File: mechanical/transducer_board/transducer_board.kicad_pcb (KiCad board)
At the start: 2 copper layers, 66.6 x 66.6 mm, 65 parts, among them J1 Conn_02x17_Odd_Even, J2 Conn_01x01, J3 Conn_01x01, J4 Conn_01x01, U1 XL62783, U2 XL62083, U3 XL62783, U4 XL62083

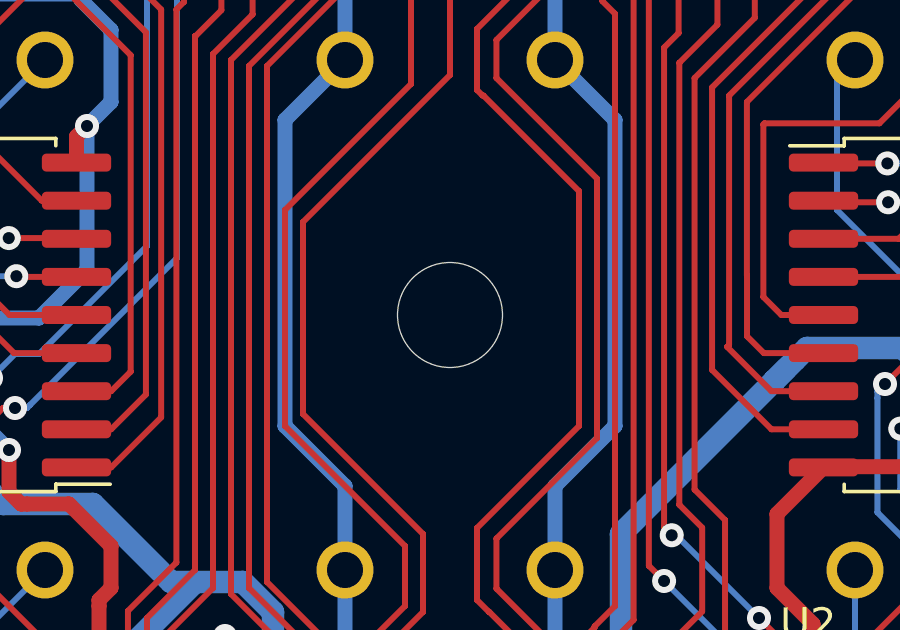
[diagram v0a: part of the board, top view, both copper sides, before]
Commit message: Tightened transducer board mounting hole size
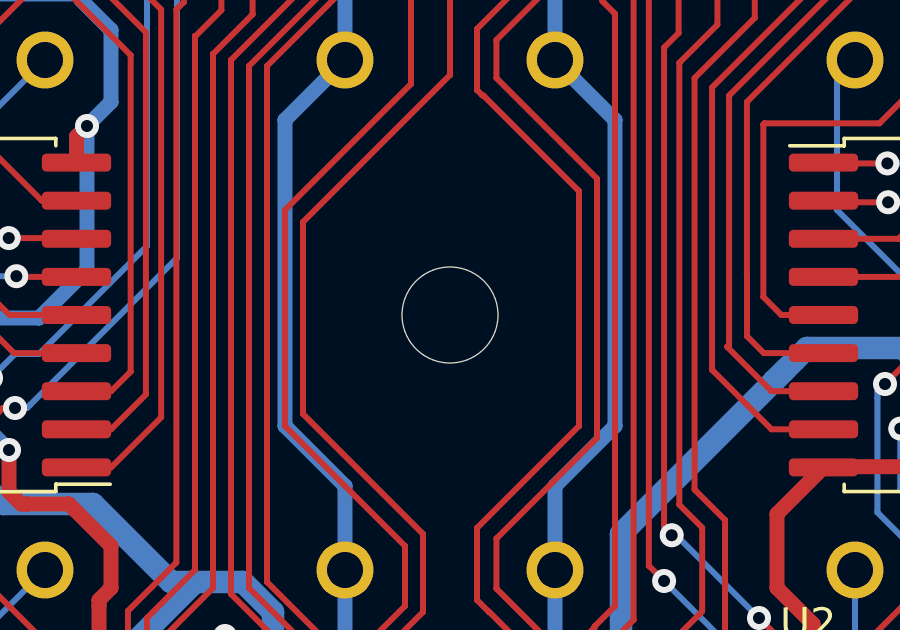
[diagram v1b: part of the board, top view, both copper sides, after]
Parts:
- REF**: value MountingHole_3.5mm -> MountingHole_3.2mm_M3; footprint MountingHole:MountingHole_3.5mm -> MountingHole:MountingHole_3.2mm_M3

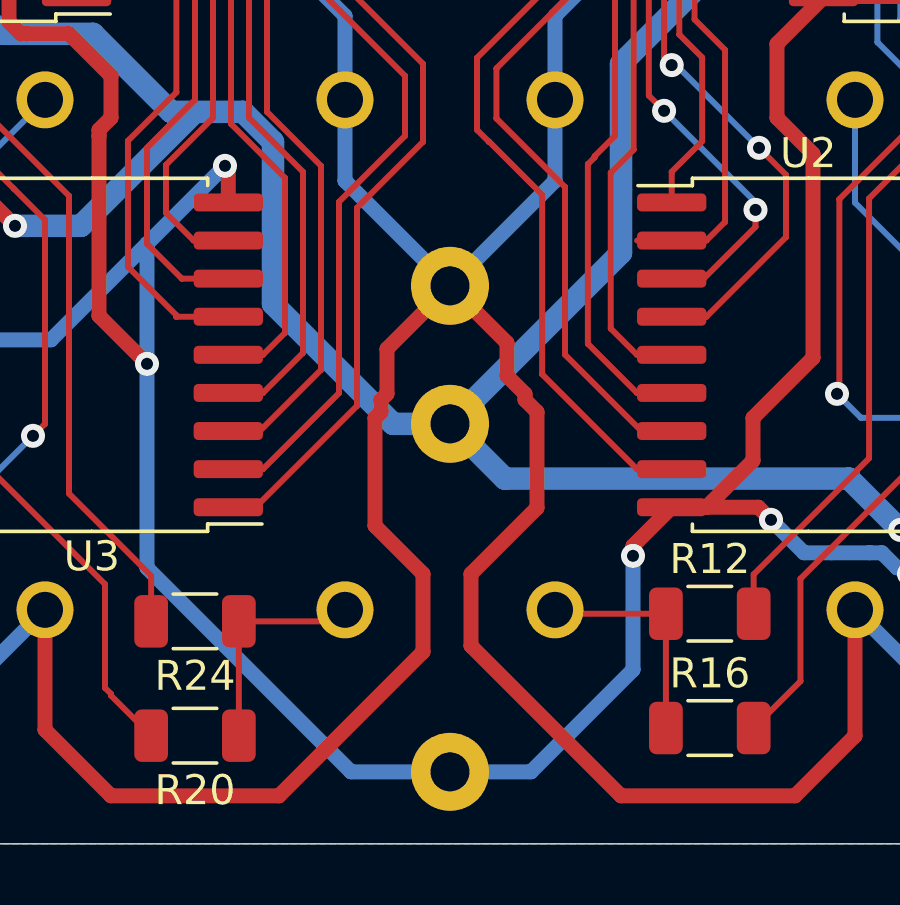
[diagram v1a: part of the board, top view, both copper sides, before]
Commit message: Clearly mark which power wire goes where
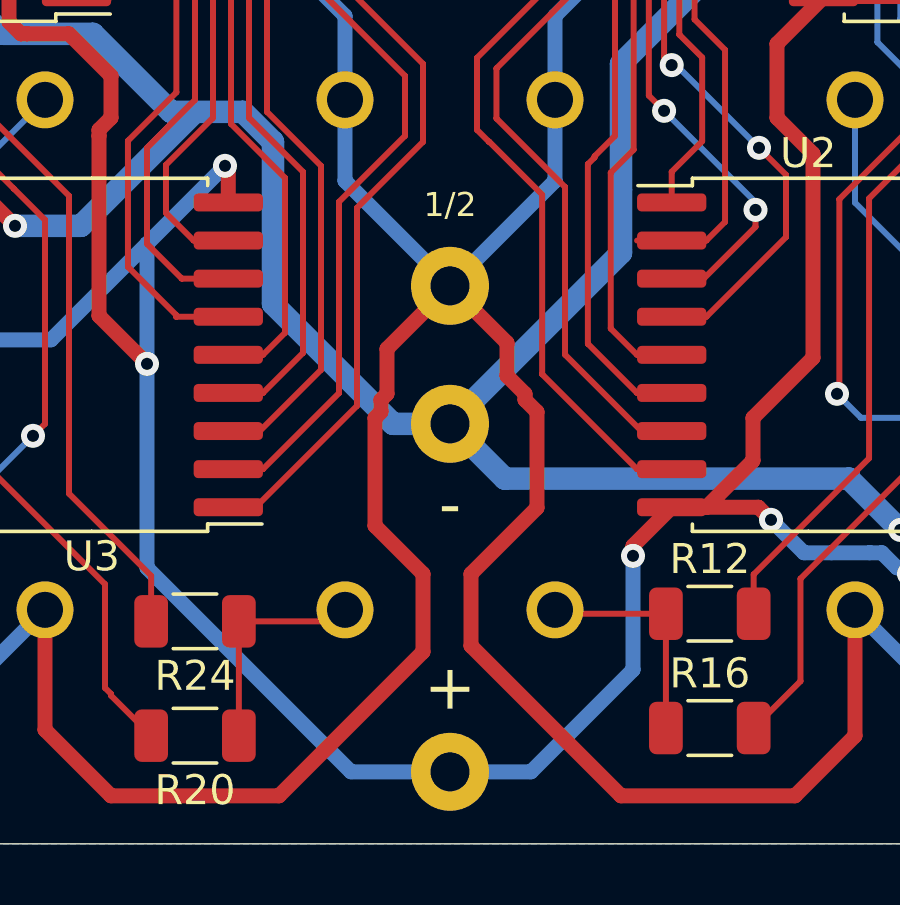
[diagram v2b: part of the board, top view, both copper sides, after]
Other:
- board text added: "+"
- board text added: "-"
- board text added: "1/2"

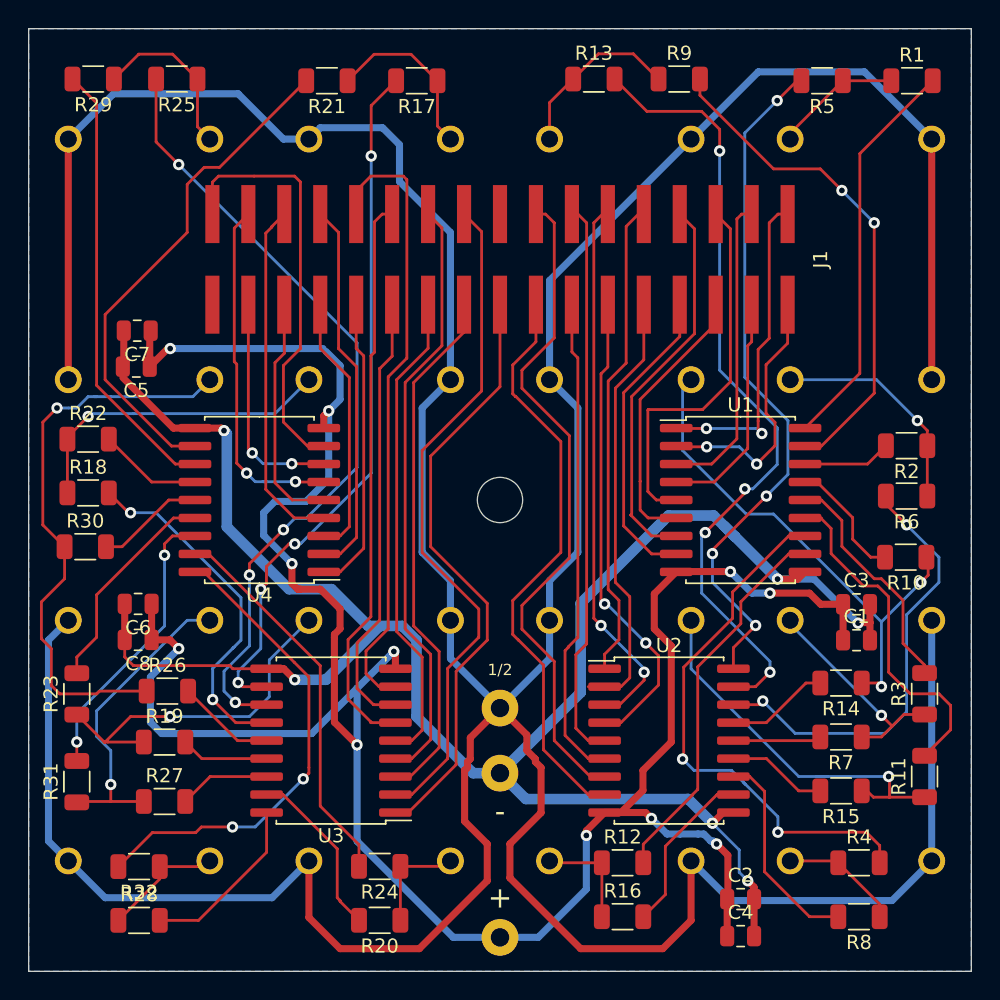
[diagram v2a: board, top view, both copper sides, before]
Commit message: increased trace thickness on transducer board
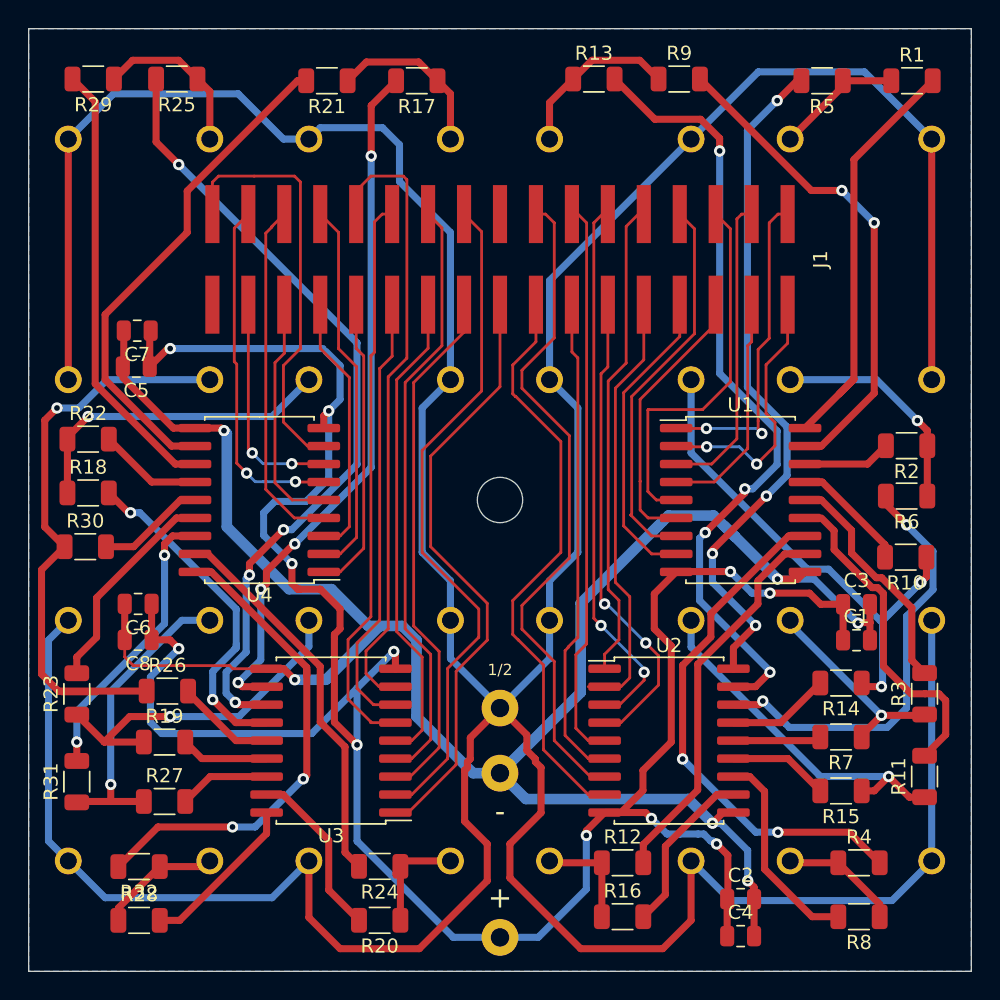
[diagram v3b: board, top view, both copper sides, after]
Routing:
- net Net-(LS6-Pad1): track 36.4 -> 44.2 mm
- net Net-(LS14-Pad1): track 40.5 -> 46.1 mm
- net Net-(LS15-Pad1): track 22.2 -> 27.5 mm
- net Net-(R1-Pad2): track 28.3 -> 33.2 mm
- net Net-(LS2-Pad1): track 15.8 -> 20.4 mm
- net Net-(LS10-Pad1): track 22.7 -> 26.6 mm
- net Net-(R18-Pad2): track 25.6 -> 29.2 mm
- net Net-(LS7-Pad1): track 27.4 -> 30.6 mm
- net Net-(R11-Pad2): track 25.4 -> 27.9 mm
- net Net-(LS3-Pad1): track 15.6 -> 14.6 mm
- net Net-(R6-Pad2): track 31.7 -> 30.8 mm
- net Net-(R28-Pad2): track 12.3 -> 11.6 mm
- net Net-(R9-Pad2): track 35.7 -> 35.0 mm
- net Net-(R32-Pad2): track 34.1 -> 34.7 mm
